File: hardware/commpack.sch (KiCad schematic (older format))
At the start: 17 parts, among them J1 1240COMM, J2 1240COMM_EXT, J3 ICSP, Q1 Q_NPN_BEC, U1 PIC16F15386, U2 74AHCT541, U3 27C128, U4 AP1117-33

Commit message: Rename project files to remove LXI mark.
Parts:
- H1, H2, H3, H4: footprint 1240comm:MountingHole_140mil_Pad -> ether1240:MountingHole_140mil_Pad
- J1: footprint 1240comm:1240COMM -> ether1240:1240COMM
- J2: footprint 1240comm:ATA_HEADER -> ether1240:ATA_HEADER
- U3: footprint (none) -> Housings_DIP:DIP-28_W15.24mm_Socket
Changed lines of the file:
@@
 EESchema Schematic File Version 2
-LIBS:1240comm
+LIBS:ether1240
 LIBS:power
 LIBS:device
@@
 LIBS:contrib
 LIBS:valves
-LIBS:microchip_pic16mcu
-LIBS:lxi1240-cache
+LIBS:commpack-cache
 EELAYER 25 0
 EELAYER END
@@
 encoding utf-8
 Sheet 1 1
-Title "LXI Comm Pack for Tektronix 1240"
+Title "Ethernet Comm Pack for Tektronix 1240"
 Date ""
 Rev ""
 Comp "© 2017 Sam Hanes <sam@maltera.com>"
 Comment1 "Licensed under CERN OHL v1.2 or later"
-Comment2 "https://github.com/Elemecca/lxi1240"
+Comment2 "https://github.com/Elemecca/ether1240"
 Comment3 ""
 Comment4 ""
@@
 F 0 "J1" V 1550 6000 60  0000 C CNN
 F 1 "1240COMM" V 1650 6000 60  0000 C CNN
-F 2 "1240comm:1240COMM" H 2050 7650 60  0001 C CNN
+F 2 "ether1240:1240COMM" H 2050 7650 60  0001 C CNN
 F 3 "" H 2050 7650 60  0001 C CNN
 	1    1650 6000
@@
 F 0 "H1" H 11000 5150 50  0000 C CNN
 F 1 "Mount" H 11000 4950 50  0000 C CNN
-F 2 "1240comm:MountingHole_140mil_Pad" H 11000 5050 50  0001 C CNN
+F 2 "ether1240:MountingHole_140mil_Pad" H 11000 5050 50  0001 C CNN
 F 3 "" H 11000 5050 50  0001 C CNN
 	1    11000 5050
@@
 F 0 "H2" H 11000 5450 50  0000 C CNN
 F 1 "Mount" H 11000 5250 50  0000 C CNN
-F 2 "1240comm:MountingHole_140mil_Pad" H 11000 5350 50  0001 C CNN
+F 2 "ether1240:MountingHole_140mil_Pad" H 11000 5350 50  0001 C CNN
 F 3 "" H 11000 5350 50  0001 C CNN
 	1    11000 5350
@@
 F 0 "H3" H 11000 5750 50  0000 C CNN
 F 1 "Mount" H 11000 5550 50  0000 C CNN
-F 2 "1240comm:MountingHole_140mil_Pad" H 11000 5650 50  0001 C CNN
+F 2 "ether1240:MountingHole_140mil_Pad" H 11000 5650 50  0001 C CNN
 F 3 "" H 11000 5650 50  0001 C CNN
 	1    11000 5650
@@
 F 0 "H4" H 11000 6050 50  0000 C CNN
 F 1 "Mount" H 11000 5850 50  0000 C CNN
-F 2 "1240comm:MountingHole_140mil_Pad" H 11000 5950 50  0001 C CNN
+F 2 "ether1240:MountingHole_140mil_Pad" H 11000 5950 50  0001 C CNN
 F 3 "" H 11000 5950 50  0001 C CNN
 	1    11000 5950
@@
 F 0 "J2" V 3750 6000 60  0000 C CNN
 F 1 "1240COMM_EXT" V 3650 6000 60  0000 C CNN
-F 2 "1240comm:ATA_HEADER" H 4050 7650 60  0001 C CNN
+F 2 "ether1240:ATA_HEADER" H 4050 7650 60  0001 C CNN
 F 3 "" H 4050 7650 60  0001 C CNN
 	1    3650 6000
@@
 F 0 "U3" H 6200 5900 50  0000 C CNN
 F 1 "27C128" H 6300 5800 50  0000 C CNN
-F 2 "" H 6100 6400 50  0001 C CNN
+F 2 "Housings_DIP:DIP-28_W15.24mm_Socket" H 6100 6400 50  0001 C CNN
 F 3 "" H 6100 6400 50  0001 C CNN
 	1    6100 6400

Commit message: Remove PIC16, add Ethernet port to schematic, fix SGND.
The PIC16 micro isn't fast enough to perform reliable bus emulation.
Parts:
- removed C1, C2: 100n, Capacitors_SMD:C_0805_HandSoldering, symbol C
- removed J3: ICSP, Pin_Headers:Pin_Header_Straight_1x06_Pitch2.54mm, symbol Conn_01x06
- removed Q1: Q_NPN_BEC, symbol Q_NPN_BEC
- removed R1: 10k, Resistors_SMD:R_0805_HandSoldering, symbol R
- removed R2: 470, Resistors_SMD:R_0805_HandSoldering, symbol R
- removed U1: PIC16F15386, Housings_QFP:TQFP-48_7x7mm_Pitch0.5mm, symbol PIC16F1538X
- removed U2: 74AHCT541, Housings_SSOP:TSSOP-20_4.4x6.5mm_Pitch0.65mm, symbol 74AHCT541
- added J3: L8BE-1G1T-91A, ether1240:L8BE-1G1T-91A, symbol L8BE-1G1T-91A
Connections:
- net labels removed: A-INT, A-SCL, A-SDA, B-D0, B-D1, B-D2, B-D3, B-D4, B-D5, B-D6, B-D7, B-PGC, B-PGD, B-~MCLR, B-~RD
- wire segments 187 -> 118
- no-connect marks 3 -> 0
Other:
- note removed: "Host Bus Interface MCU"

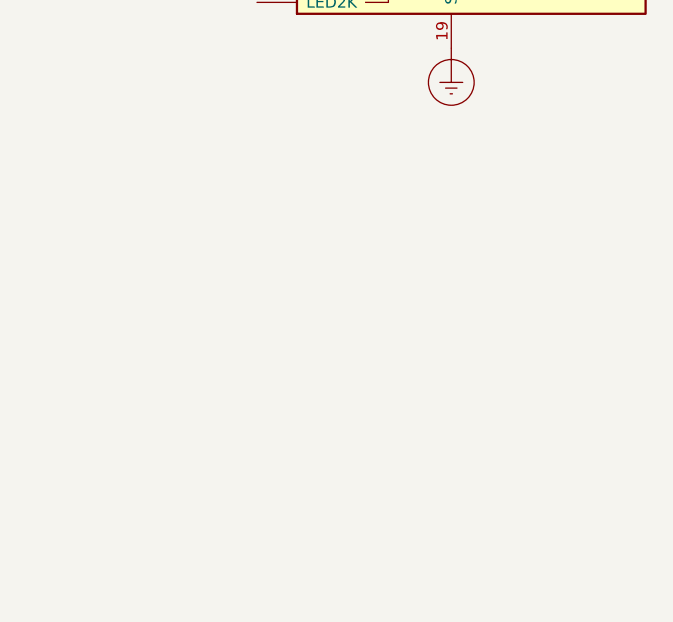
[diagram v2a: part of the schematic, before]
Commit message: Add USB-B connector.
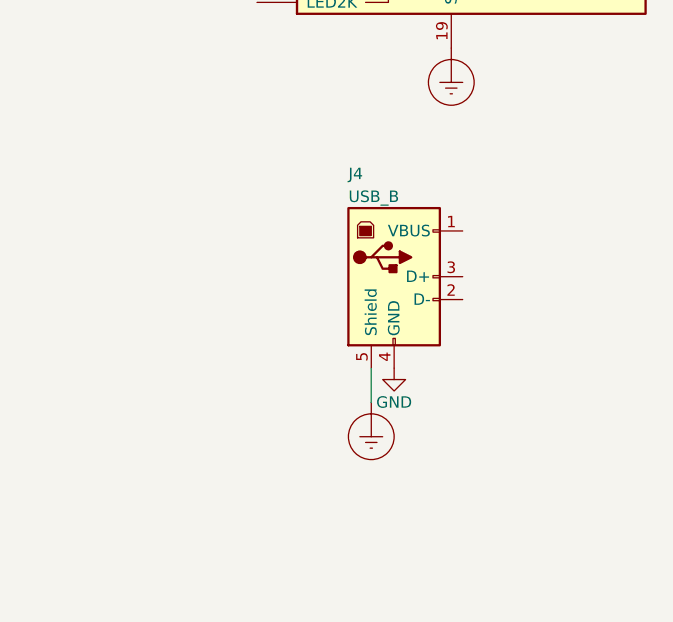
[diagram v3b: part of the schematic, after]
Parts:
- added J4: USB_B, ether1240:USB-B, symbol USB_B
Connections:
- wire segments 118 -> 119
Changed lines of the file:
@@
 	1    0    0    -1
 $EndComp
+$Comp
+L USB_B J4
+U 1 1 5A147DBB
+P 10000 3050
+F 0 "J4" H 9800 3500 50  0000 L CNN
+F 1 "USB_B" H 9800 3400 50  0000 L CNN
+F 2 "ether1240:USB-B" H 10150 3000 50  0001 C CNN
+F 3 "" H 10150 3000 50  0001 C CNN
+	1    10000 3050
+	1    0    0    -1
+$EndComp
+$Comp
+L GND #PWR019
+U 1 1 5A14807A
+P 10000 3450
+F 0 "#PWR019" H 10000 3200 50  0001 C CNN
+F 1 "GND" H 10000 3300 50  0000 C CNN
+F 2 "" H 10000 3450 50  0001 C CNN
+F 3 "" H 10000 3450 50  0001 C CNN
+	1    10000 3450
+	1    0    0    -1
+$EndComp
+$Comp
+L Earth_Protective #PWR020
+U 1 1 5A1480A4
+P 9900 3600
+F 0 "#PWR020" H 10150 3350 50  0001 C CNN
+F 1 "Earth_Protective" H 10350 3450 50  0001 C CNN
+F 2 "" H 9900 3500 50  0001 C CNN
+F 3 "" H 9900 3500 50  0001 C CNN
+	1    9900 3600
+	1    0    0    -1
+$EndComp
+Wire Wire Line
+	9900 3600 9900 3450
 $EndSCHEMATC

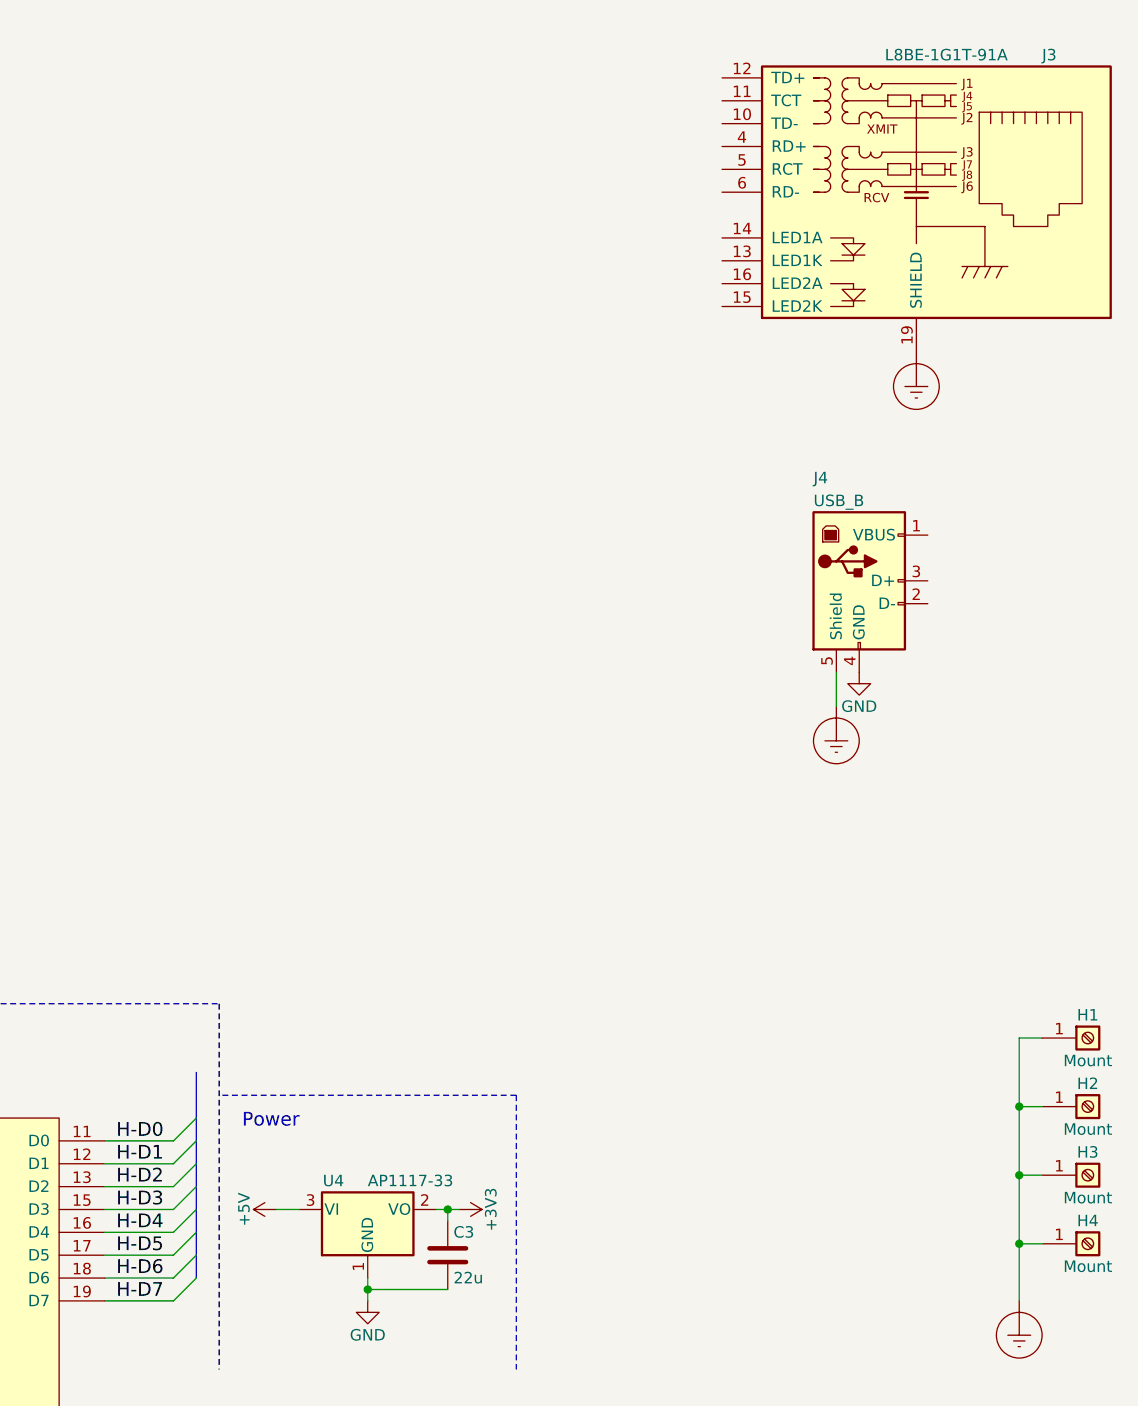
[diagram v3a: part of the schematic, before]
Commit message: Add Omega2 footprint to board.
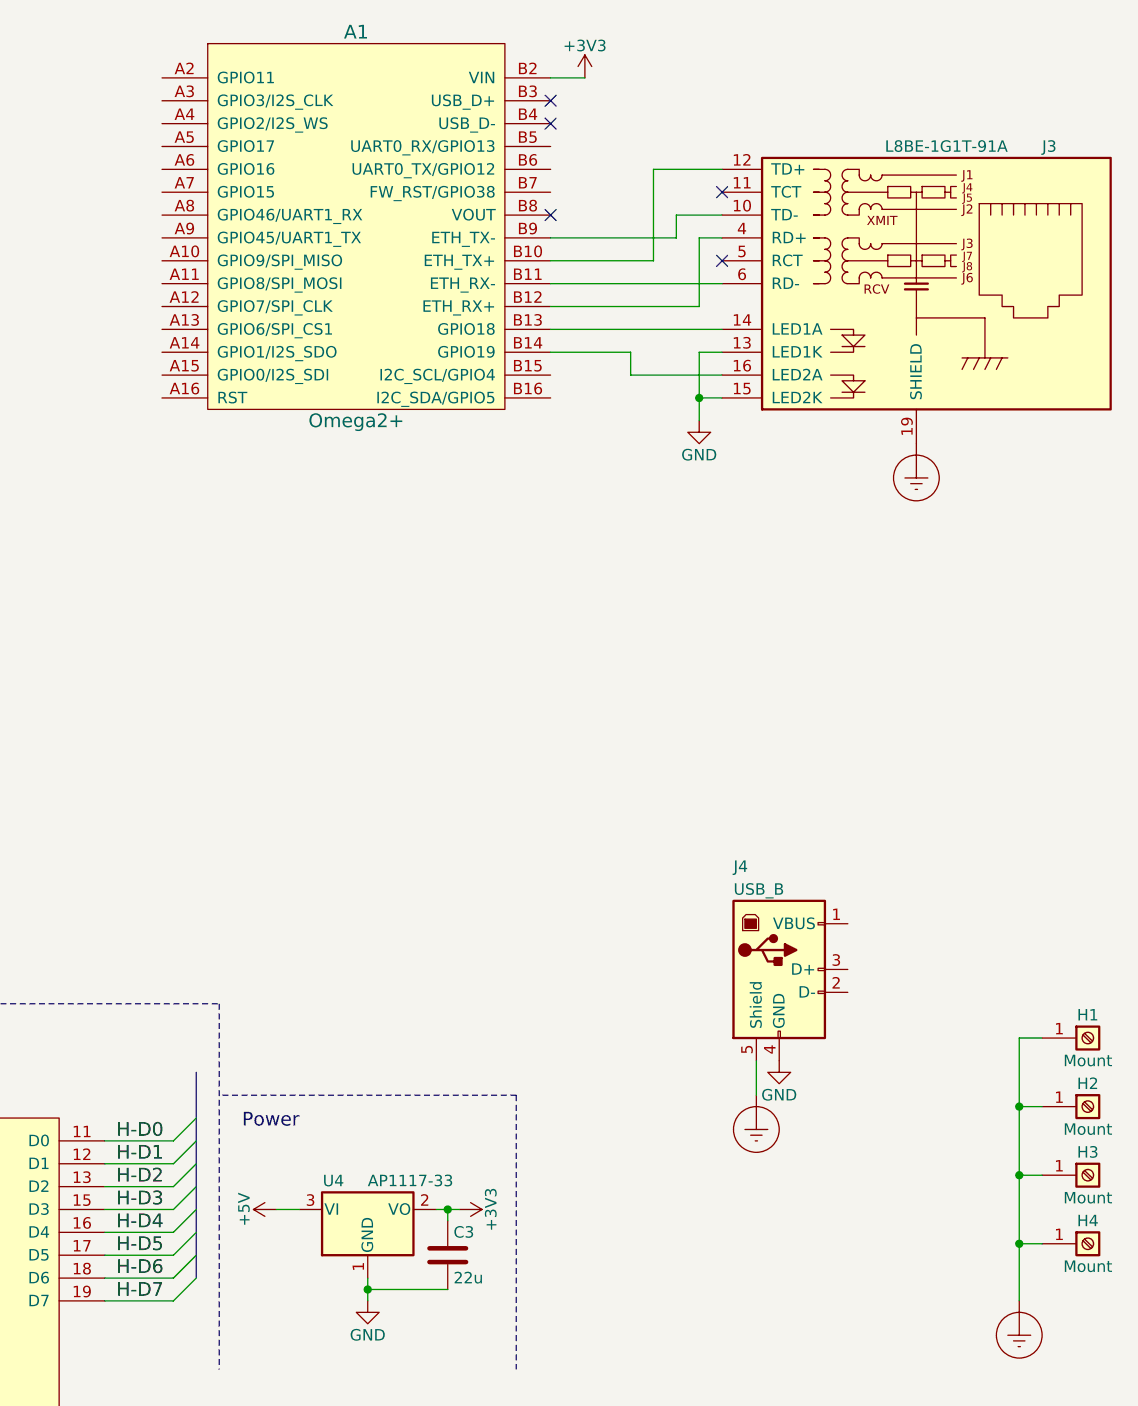
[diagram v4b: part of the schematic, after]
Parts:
- added A1: Omega2+, ether1240:Omega2, symbol Omega2+
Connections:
- wire segments 119 -> 137
- no-connect marks 0 -> 5
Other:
- moved on the sheet: J3, J4

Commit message: Change ATA pinout, rip up EPROM socket and Omega2.
I missed two grounded pins when I did the original ATA connector pinout,
so this drops the +12V and -12V connections and rearranges everything to
avoid shorting two of the address lines to ground.
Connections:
- net labels removed: +12VA, -12VA
- wire segments 137 -> 123
- no-connect marks 5 -> 7
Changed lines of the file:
@@
 Comment4 ""
 $EndDescr
-$Comp
-L 1240COMM J1
-U 1 1 59FE52B4
-P 1650 6000
-F 0 "J1" V 1550 6000 60  0000 C CNN
-F 1 "1240COMM" V 1650 6000 60  0000 C CNN
-F 2 "ether1240:1240COMM" H 2050 7650 60  0001 C CNN
-F 3 "" H 2050 7650 60  0001 C CNN
-	1    1650 6000
-	1    0    0    -1
-$EndComp
 Entry Wire Line
 	2550 5700 2650 5800
@@
 	550  6000 650  6100
 $Comp
-L -12VA #PWR01
-U 1 1 59FE53EC
-P 1700 7300
-F 0 "#PWR01" H 1700 7150 50  0001 C CNN
-F 1 "-12VA" H 1700 7440 50  0000 C CNN
-F 2 "" H 1700 7300 50  0001 C CNN
-F 3 "" H 1700 7300 50  0001 C CNN
-	1    1700 7300
-	1    0    0    -1
-$EndComp
-$Comp
-L GND #PWR02
+L GND #PWR01
 U 1 1 59FE545B
 P 1450 7400
-F 0 "#PWR02" H 1450 7150 50  0001 C CNN
+F 0 "#PWR01" H 1450 7150 50  0001 C CNN
 F 1 "GND" H 1450 7250 50  0000 C CNN
 F 2 "" H 1450 7400 50  0001 C CNN
@@
 $EndComp
 $Comp
-L Earth_Protective #PWR03
+L Earth_Protective #PWR02
 U 1 1 59FE5473
 P 1200 7400
-F 0 "#PWR03" H 1450 7150 50  0001 C CNN
+F 0 "#PWR02" H 1450 7150 50  0001 C CNN
 F 1 "Earth_Protective" H 1650 7250 50  0001 C CNN
 F 2 "" H 1200 7300 50  0001 C CNN
 F 3 "" H 1200 7300 50  0001 C CNN
 	1    1200 7400
-	1    0    0    -1
-$EndComp
-$Comp
-L +12VA #PWR04
-U 1 1 59FE54FB
-P 1450 4700
-F 0 "#PWR04" H 1450 4550 50  0001 C CNN
-F 1 "+12VA" H 1450 4840 50  0000 C CNN
-F 2 "" H 1450 4700 50  0001 C CNN
-F 3 "" H 1450 4700 50  0001 C CNN
-	1    1450 4700
-	1    0    0    -1
-$EndComp
-$Comp
-L +5V #PWR05
-U 1 1 59FE5511
-P 1700 4700
-F 0 "#PWR05" H 1700 4550 50  0001 C CNN
-F 1 "+5V" H 1700 4840 50  0000 C CNN
-F 2 "" H 1700 4700 50  0001 C CNN
-F 3 "" H 1700 4700 50  0001 C CNN
-	1    1700 4700
 	1    0    0    -1
 $EndComp
@@
 H-D7
 $Comp
-L GND #PWR06
+L GND #PWR03
 U 1 1 59FE6FF1
 P 3850 7400
-F 0 "#PWR06" H 3850 7150 50  0001 C CNN
+F 0 "#PWR03" H 3850 7150 50  0001 C CNN
 F 1 "GND" H 3850 7250 50  0000 C CNN
 F 2 "" H 3850 7400 50  0001 C CNN
@@
 $EndComp
 $Comp
-L Earth_Protective #PWR07
+L Earth_Protective #PWR04
 U 1 1 59FE6FF7
 P 4100 7400
-F 0 "#PWR07" H 4350 7150 50  0001 C CNN
+F 0 "#PWR04" H 4350 7150 50  0001 C CNN
 F 1 "Earth_Protective" H 4550 7250 50  0001 C CNN
 F 2 "" H 4100 7300 50  0001 C CNN
 F 3 "" H 4100 7300 50  0001 C CNN
 	1    4100 7400
-	-1   0    0    -1
-$EndComp
-$Comp
-L -12VA #PWR08
-U 1 1 59FE7014
-P 3500 7300
-F 0 "#PWR08" H 3500 7150 50  0001 C CNN
-F 1 "-12VA" H 3500 7440 50  0000 C CNN
-F 2 "" H 3500 7300 50  0001 C CNN
-F 3 "" H 3500 7300 50  0001 C CNN
-	1    3500 7300
-	1    0    0    -1
-$EndComp
-$Comp
-L +12VA #PWR09
-U 1 1 59FE7200
-P 3850 4700
-F 0 "#PWR09" H 3850 4550 50  0001 C CNN
-F 1 "+12VA" H 3850 4840 50  0000 C CNN
-F 2 "" H 3850 4700 50  0001 C CNN
-F 3 "" H 3850 4700 50  0001 C CNN
-	1    3850 4700
-	-1   0    0    -1
-$EndComp
-$Comp
-L +5V #PWR010
-U 1 1 59FE7206
-P 3600 4700
-F 0 "#PWR010" H 3600 4550 50  0001 C CNN
-F 1 "+5V" H 3600 4840 50  0000 C CNN
-F 2 "" H 3600 4700 50  0001 C CNN
-F 3 "" H 3600 4700 50  0001 C CNN
-	1    3600 4700
 	-1   0    0    -1
 $EndComp
@@
 $EndComp
 $Comp
-L Earth_Protective #PWR011
+L Earth_Protective #PWR05
 U 1 1 59FEBA57
 P 10700 6200
-F 0 "#PWR011" H 10950 5950 50  0001 C CNN
+F 0 "#PWR05" H 10950 5950 50  0001 C CNN
 F 1 "Earth_Protective" H 11150 6050 50  0001 C CNN
 F 2 "" H 10700 6100 50  0001 C CNN
 F 3 "" H 10700 6100 50  0001 C CNN
 	1    10700 6200
-	1    0    0    -1
-$EndComp
-$Comp
-L 1240COMM_EXT J2
-U 1 1 5A02D637
-P 3650 6000
-F 0 "J2" V 3750 6000 60  0000 C CNN
-F 1 "1240COMM_EXT" V 3650 6000 60  0000 C CNN
-F 2 "ether1240:ATA_HEADER" H 4050 7650 60  0001 C CNN
-F 3 "" H 4050 7650 60  0001 C CNN
-	1    3650 6000
 	1    0    0    -1
 $EndComp
@@
 H-~RD
 $Comp
-L +5V #PWR012
+L +5V #PWR06
 U 1 1 5A017DF5
 P 5500 7000
-F 0 "#PWR012" H 5500 6850 50  0001 C CNN
+F 0 "#PWR06" H 5500 6850 50  0001 C CNN
 F 1 "+5V" H 5500 7140 50  0000 C CNN
 F 2 "" H 5500 7000 50  0001 C CNN
@@
 $EndComp
 $Comp
-L +3V3 #PWR013
+L +3V3 #PWR07
 U 1 1 5A02C4F9
 P 8250 5800
-F 0 "#PWR013" H 8250 5650 50  0001 C CNN
+F 0 "#PWR07" H 8250 5650 50  0001 C CNN
 F 1 "+3V3" H 8250 5940 50  0000 C CNN
 F 2 "" H 8250 5800 50  0001 C CNN
@@
 $EndComp
 $Comp
-L +5V #PWR014
+L +5V #PWR08
 U 1 1 5A02C685
 P 7450 5800
-F 0 "#PWR014" H 7450 5650 50  0001 C CNN
+F 0 "#PWR08" H 7450 5650 50  0001 C CNN
 F 1 "+5V" H 7450 5940 50  0000 C CNN
 F 2 "" H 7450 5800 50  0001 C CNN
@@
 $EndComp
 $Comp
-L GND #PWR015
+L GND #PWR09
 U 1 1 5A02CAF9
 P 7850 6200
-F 0 "#PWR015" H 7850 5950 50  0001 C CNN
+F 0 "#PWR09" H 7850 5950 50  0001 C CNN
 F 1 "GND" H 7850 6050 50  0000 C CNN
 F 2 "" H 7850 6200 50  0001 C CNN
@@
 $EndComp
 $Comp
-L GND #PWR016
+L GND #PWR010
 U 1 1 5A030543
 P 6100 7600
-F 0 "#PWR016" H 6100 7350 50  0001 C CNN
+F 0 "#PWR010" H 6100 7350 50  0001 C CNN
 F 1 "GND" H 6100 7450 50  0000 C CNN
 F 2 "" H 6100 7600 50  0001 C CNN
@@
 $EndComp
 $Comp
-L +5V #PWR017
+L +5V #PWR011
 U 1 1 5A0305F0
 P 6100 5200
-F 0 "#PWR017" H 6100 5050 50  0001 C CNN
+F 0 "#PWR011" H 6100 5050 50  0001 C CNN
 F 1 "+5V" H 6100 5340 50  0000 C CNN
 F 2 "" H 6100 5200 50  0001 C CNN
@@
 $EndComp
 $Comp
-L Earth_Protective #PWR018
+L Earth_Protective #PWR012
 U 1 1 5A1473A0
 P 10250 2450
-F 0 "#PWR018" H 10500 2200 50  0001 C CNN
+F 0 "#PWR012" H 10500 2200 50  0001 C CNN
 F 1 "Earth_Protective" H 10700 2300 50  0001 C CNN
 F 2 "" H 10250 2350 50  0001 C CNN
@@
 $EndComp
 $Comp
-L GND #PWR019
+L GND #PWR013
 U 1 1 5A14807A
 P 9650 5150
-F 0 "#PWR019" H 9650 4900 50  0001 C CNN
+F 0 "#PWR013" H 9650 4900 50  0001 C CNN
 F 1 "GND" H 9650 5000 50  0000 C CNN
 F 2 "" H 9650 5150 50  0001 C CNN
@@
 $EndComp
 $Comp
-L Earth_Protective #PWR020
+L Earth_Protective #PWR014
 U 1 1 5A1480A4
 P 9550 5300
-F 0 "#PWR020" H 9800 5050 50  0001 C CNN
+F 0 "#PWR014" H 9800 5050 50  0001 C CNN
 F 1 "Earth_Protective" H 10000 5150 50  0001 C CNN
 F 2 "" H 9550 5200 50  0001 C CNN
@@
 $EndComp
 $Comp
-L +3V3 #PWR021
+L +3V3 #PWR015
 U 1 1 5A1FFA04
 P 8800 850
-F 0 "#PWR021" H 8800 700 50  0001 C CNN
+F 0 "#PWR015" H 8800 700 50  0001 C CNN
 F 1 "+3V3" H 8800 990 50  0000 C CNN
 F 2 "" H 8800 850 50  0001 C CNN
@@
 	1350 4800 1350 4700
 Wire Wire Line
-	3600 4750 3600 4700
-Wire Wire Line
-	3750 4750 3600 4750
-Wire Wire Line
-	3750 4800 3750 4750
-Wire Wire Line
-	3850 4800 3850 4700
-Wire Wire Line
-	3500 7350 3500 7300
-Wire Wire Line
 	4100 7350 4100 7400
 Wire Wire Line
@@
 	3850 7300 3850 7400
 Wire Wire Line
-	3500 7350 3750 7350
-Wire Wire Line
-	3750 7350 3750 7300
-Wire Wire Line
 	4250 6100 4650 6100
 Wire Wire Line
@@
 Wire Wire Line
 	3150 5700 2750 5700
-Wire Wire Line
-	1700 7350 1700 7300
 Wire Bus Line
 	2650 5800 2650 7350
@@
 	1200 7350 1200 7400
 Wire Wire Line
-	1700 4750 1700 4700
-Wire Wire Line
-	1550 4750 1700 4750
-Wire Wire Line
-	1550 4800 1550 4750
-Wire Wire Line
-	1450 4800 1450 4700
-Wire Wire Line
 	1350 7350 1200 7350
 Wire Wire Line
@@
 Wire Wire Line
 	1450 7300 1450 7400
-Wire Wire Line
-	1550 7350 1700 7350
-Wire Wire Line
-	1550 7300 1550 7350
 Wire Wire Line
 	1050 6100 650  6100
@@
 Connection ~ 9300 2250
 $Comp
-L GND #PWR022
+L GND #PWR016
 U 1 1 5A2003A7
 P 9300 2350
-F 0 "#PWR022" H 9300 2100 50  0001 C CNN
+F 0 "#PWR016" H 9300 2100 50  0001 C CNN
 F 1 "GND" H 9300 2200 50  0000 C CNN
 F 2 "" H 9300 2350 50  0001 C CNN
@@
 NoConn ~ 8650 950
 NoConn ~ 8650 1050
+$Comp
+L 1240COMM_EXT J2
+U 1 1 5A02D637
+P 3650 6000
+F 0 "J2" V 3750 6000 60  0000 C CNN
+F 1 "1240COMM_EXT" V 3650 6000 60  0000 C CNN
+F 2 "ether1240:ATA_HEADER" H 4050 7650 60  0001 C CNN
+F 3 "" H 4050 7650 60  0001 C CNN
+	1    3650 6000
+	1    0    0    -1
+$EndComp
+$Comp
+L +5V #PWR017
+U 1 1 59FE7206
+P 3850 4800
+F 0 "#PWR017" H 3850 4650 50  0001 C CNN
+F 1 "+5V" H 3850 4940 50  0000 C CNN
+F 2 "" H 3850 4800 50  0001 C CNN
+F 3 "" H 3850 4800 50  0001 C CNN
+	1    3850 4800
+	-1   0    0    -1
+$EndComp
+$Comp
+L +5V #PWR018
+U 1 1 59FE5511
+P 1550 4800
+F 0 "#PWR018" H 1550 4650 50  0001 C CNN
+F 1 "+5V" H 1550 4940 50  0000 C CNN
+F 2 "" H 1550 4800 50  0001 C CNN
+F 3 "" H 1550 4800 50  0001 C CNN
+	1    1550 4800
+	1    0    0    -1
+$EndComp
+NoConn ~ 1450 4800
+$Comp
+L 1240COMM J1
+U 1 1 59FE52B4
+P 1650 6000
+F 0 "J1" V 1550 6000 60  0000 C CNN
+F 1 "1240COMM" V 1650 6000 60  0000 C CNN
+F 2 "ether1240:1240COMM" H 2050 7650 60  0001 C CNN
+F 3 "" H 2050 7650 60  0001 C CNN
+	1    1650 6000
+	1    0    0    -1
+$EndComp
+NoConn ~ 1550 7300
 $EndSCHEMATC
